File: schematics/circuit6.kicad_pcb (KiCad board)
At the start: 2 copper layers, 19.8 x 16.8 mm, 14 parts

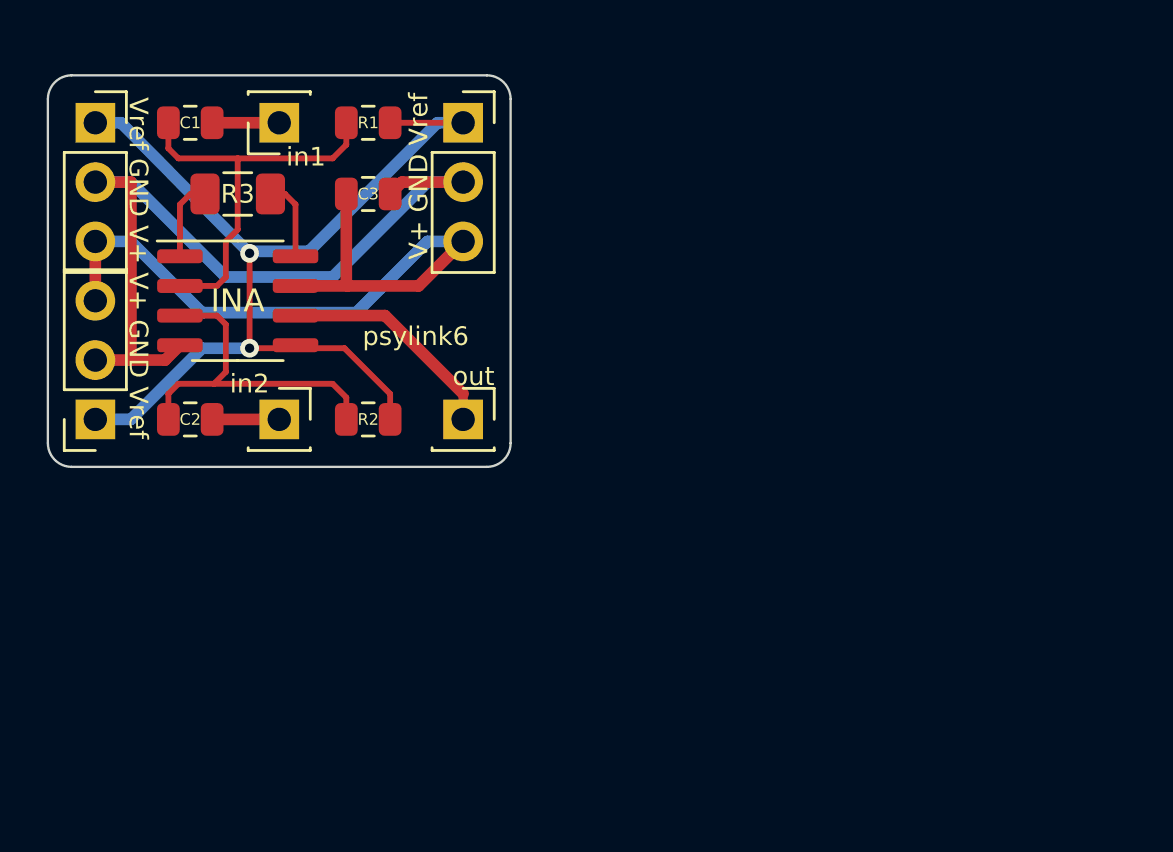
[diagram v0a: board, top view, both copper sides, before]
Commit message: rename circuits/PCBs
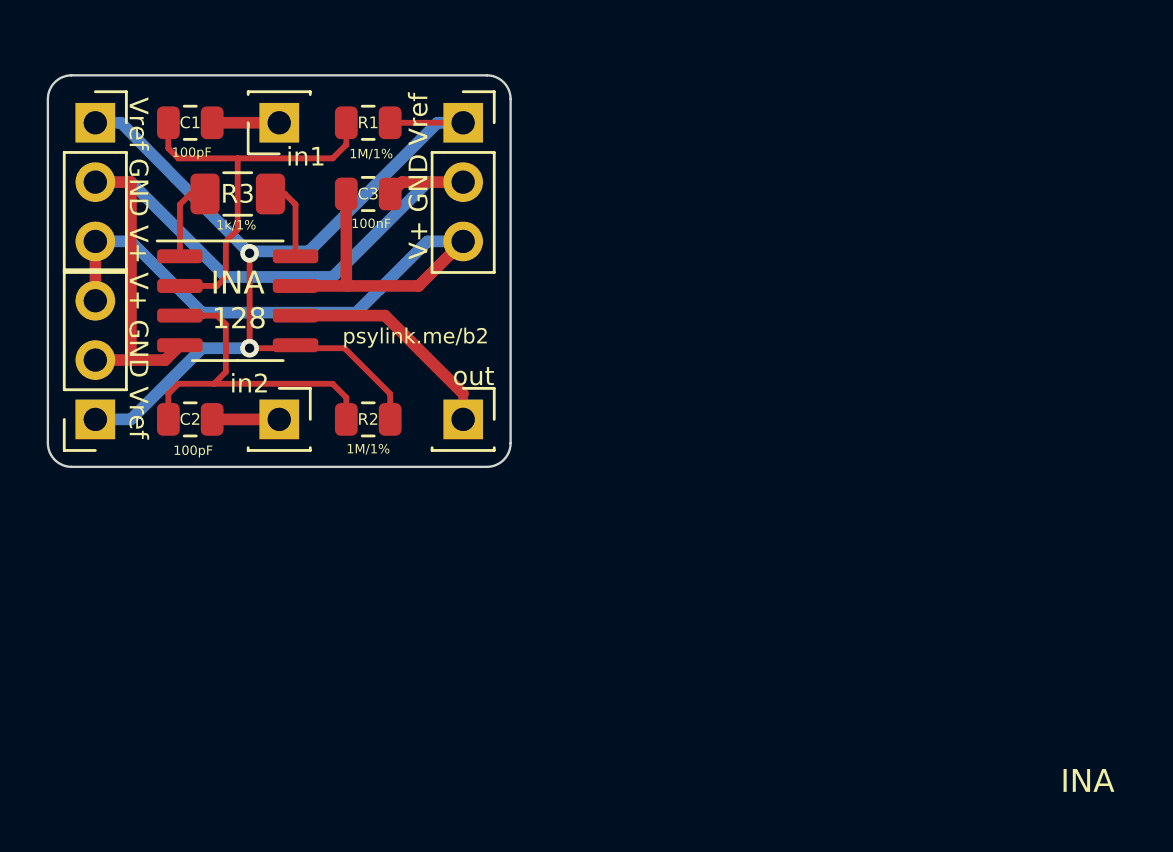
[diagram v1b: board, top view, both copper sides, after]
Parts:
- added ?: , , F.Cu at (26.7, 28.4)
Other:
- board text added: "100nF"
- board text added: "100pF"
- board text added: "128"
- board text added: "1M/1%"
- board text added: "1k/1%"
- board text added: "psylink.me/b2"
- board text removed: "psylink6"
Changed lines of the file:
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@@
   (general
     (thickness 1.6)
-    (drawings 14)
+    (drawings 21)
     (tracks 75)
     (zones 0)
-    (modules 14)
+    (modules 15)
     (nets 1)
   )
@@
     (uvia_drill 0.1)
   )
+  (module "" (layer F.Cu)
+    (at 26.67 28.448)
+    (fp_text reference "" (at 36.576 20.32) (layer F.SilkS)
+      (effects (font (size 1.27 1.27) (thickness 0.15)))
+    )
+    (fp_text value "" (at 36.576 20.32) (layer F.SilkS)
+      (effects (font (size 1.27 1.27) (thickness 0.15)))
+    )
+    (fp_text user INA (at 36.6395 20.066) (layer F.SilkS)
+      (effects (font (size 0.98 0.98) (thickness 0.15)))
+    )
+  )
   (module Connector_PinSocket_2.54mm:PinSocket_1x03_P2.54mm_Vertical (layer F.Cu)
     (at 36.576 20.32)
@@
       (effects (font (size 1 1) (thickness 0.15)))
     )
-    (fp_text user INA (at 0 0) (layer F.SilkS)
+    (fp_text user INA (at 0 -0.762) (layer F.SilkS)
       (effects (font (size 0.98 0.98) (thickness 0.15)))
     )
@@
     )
   )
+  (gr_text 128 (at 26.9875 28.702) (layer F.SilkS)
+    (effects (font (size 0.9 0.9) (thickness 0.13)))
+  )
+  (gr_text 1k/1% (at 26.8605 24.7015) (layer F.SilkS)
+    (effects (font (size 0.4 0.4) (thickness 0.05)))
+  )
+  (gr_text 1M/1% (at 32.512 34.29) (layer F.SilkS)
+    (effects (font (size 0.4 0.4) (thickness 0.05)))
+  )
+  (gr_text 1M/1% (at 32.639 21.6535) (layer F.SilkS)
+    (effects (font (size 0.4 0.4) (thickness 0.05)))
+  )
+  (gr_text 100nF (at 32.639 24.638) (layer F.SilkS)
+    (effects (font (size 0.4 0.4) (thickness 0.05)))
+  )
+  (gr_text 100pF (at 25.019 34.3535) (layer F.SilkS)
+    (effects (font (size 0.4 0.4) (thickness 0.05)))
+  )
+  (gr_text 100pF (at 24.9555 21.59) (layer F.SilkS)
+    (effects (font (size 0.4 0.4) (thickness 0.05)))
+  )
   (gr_text out (at 37.0205 31.1785) (layer F.SilkS)
     (effects (font (size 0.8 0.8) (thickness 0.1)))
@@
   (gr_arc (start 19.812 19.304) (end 19.812 18.288) (angle -90) (layer Edge.Cuts) (width 0.1))
   (gr_arc (start 37.592 19.304) (end 38.608 19.304) (angle -90) (layer Edge.Cuts) (width 0.1))
-  (gr_text psylink6 (at 34.544 29.464) (layer F.SilkS)
-    (effects (font (size 0.8 0.8) (thickness 0.1)))
+  (gr_text psylink.me/b2 (at 34.544 29.464) (layer F.SilkS)
+    (effects (font (size 0.65 0.65) (thickness 0.1)))
   )
   (gr_line (start 38.608 19.304) (end 38.608 34.036) (layer Edge.Cuts) (width 0.1))
